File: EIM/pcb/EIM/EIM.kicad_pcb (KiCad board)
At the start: 2 copper layers, 170.6 x 136.2 mm, 249 parts, among them IC1 TLIN1027DRQ1, IC10 ILD213T, IC2 SN65HVD1780QDRQ1, IC3 ILD213T, IC4 ILD213T, IC5 ILD213T, IC6 ILD213T, IC7 ILD213T, IC8 ILD213T, IC9 ILD213T, J1 MX34028NF2, J2 36783-1201, J3 34830-0801, J4 34830-2001, J5 DEBUG1, J6 DEBUG2, J7 FTSH-107-01-F-DV-K, J8 SWD, K1 G8N-1L-AS_DC12, Q1 BSS138, Q2 BSS138, Q3 BSS138, Q4 BSS138, Q5 BSS138, Q6 BSS138, Q7 BSS138, SW1 BOOT, SW2 RESET, U1 STM32F429ZITx, U10 BTS6142D, U11 BTS6142D, U12 BTS6142D, U2 AP63200WU, U3 AP63203WU, U4 SN65HVD233, U5 SN65HVD233, U6 BTS6142D, U7 BTS6142D, U8 BTS6142D, U9 BTS6142D, X1 ASE-8.000MHz, X2 ECS-327-32.768kHz

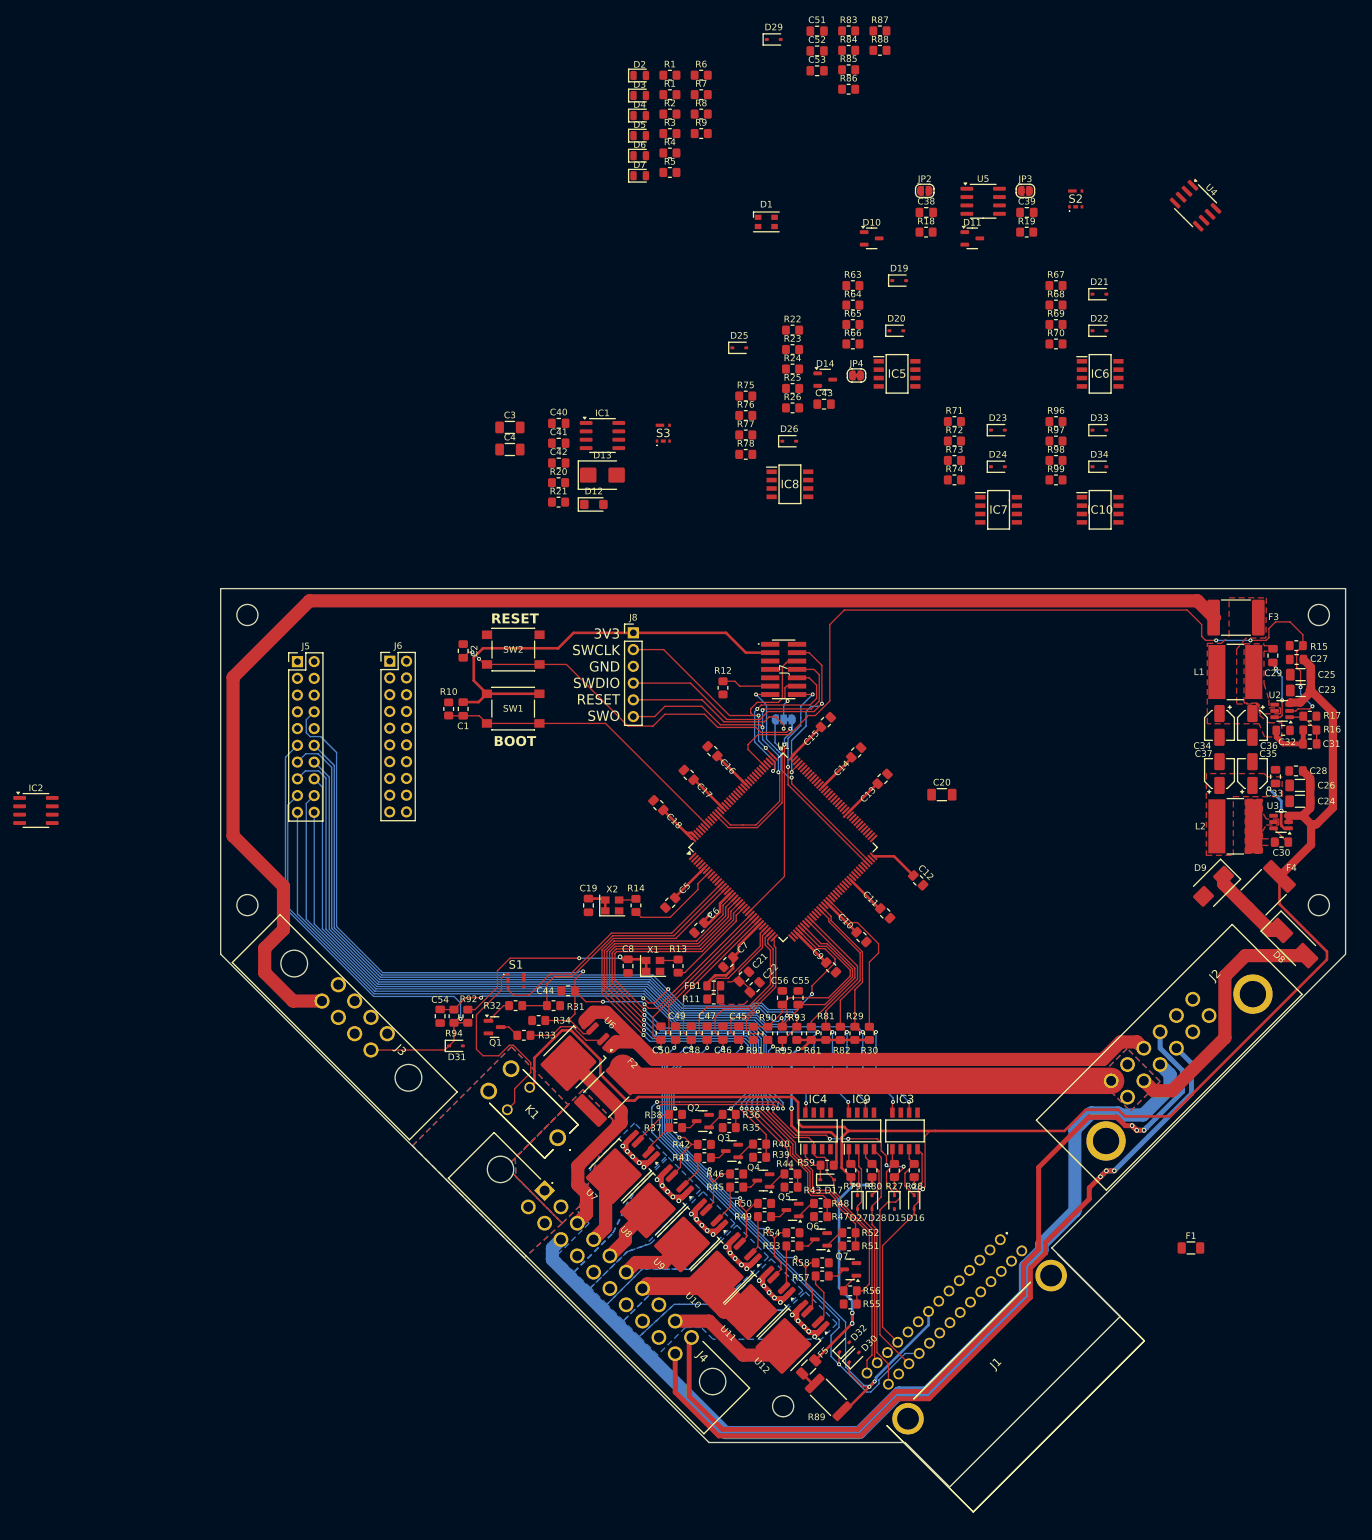
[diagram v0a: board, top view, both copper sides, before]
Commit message: All components placed and pins assigned.
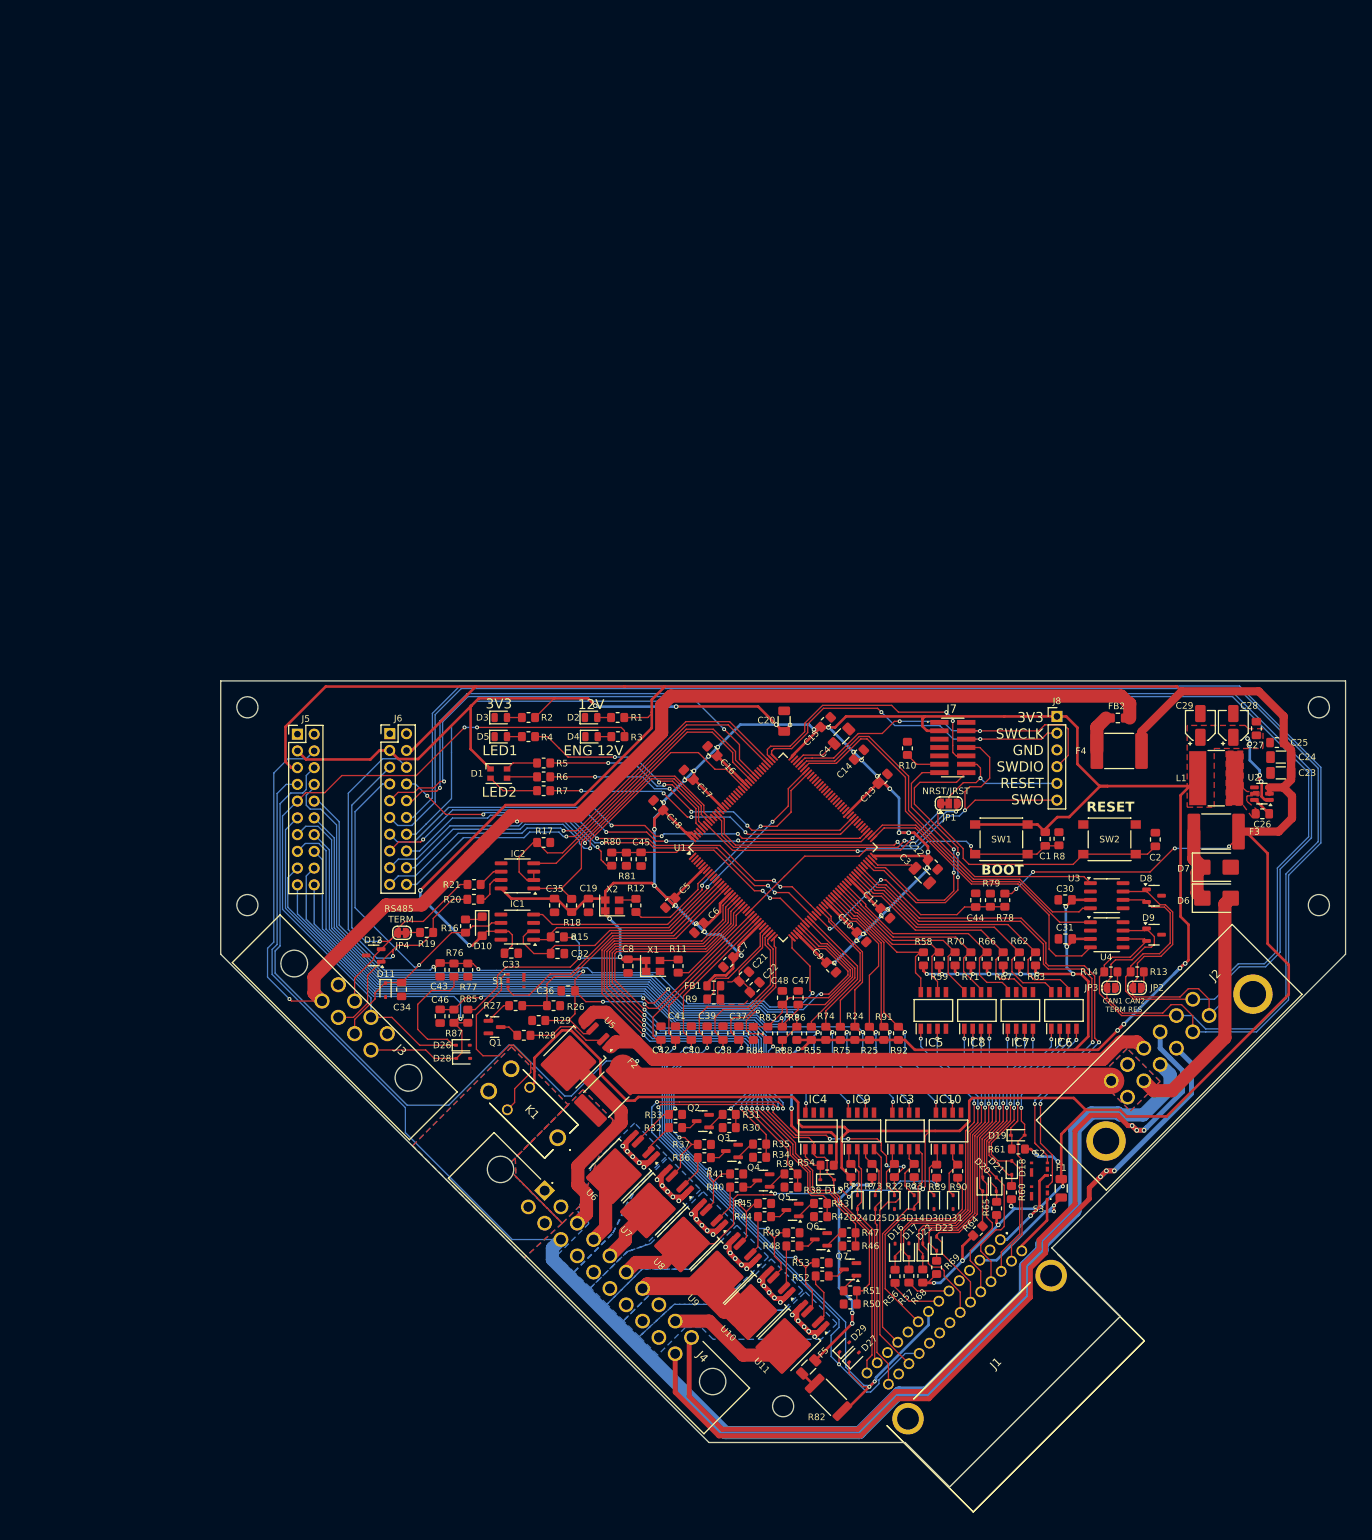
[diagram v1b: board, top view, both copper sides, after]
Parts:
- removed the C23 at (191.8, 66.2)
- removed the C25 at (191.8, 63.8)
- removed the C27 at (191.2, 61.5)
- removed the C29 at (187.6, 60.9)
- removed the C31 at (193.2, 74.3)
- removed the C32 at (189.2, 72.2)
- removed the C34 at (179.5, 71.5)
- removed the C36 at (184.5, 71.5)
- removed C53: 100n, Capacitor_SMD:C_0805_2012Metric_Pad1.18x1.45mm_HandSolder
- removed the D13 at (85.9, 33.5)
- removed the D3 at (91.6, -24.0)
- removed the D5 at (91.6, -17.9)
- removed the F3 at (182.0, 55.1)
- removed the L1 at (181.9, 63.4)
- removed the R1 at (96.2, -27.1)
- removed the R15 at (191.2, 59.4)
- removed the R16 at (193.2, 72.2)
- removed the R17 at (193.2, 70.1)
- removed the R2 at (96.2, -21.2)
- removed the R4 at (96.2, -15.3)
- removed the R87 at (128.0, -33.8)
- removed the R88 at (128.0, -30.9)
- removed the U2 at (189.0, 69.3)
- added C45: 100n, Capacitor_SMD:C_0805_2012Metric_Pad1.18x1.45mm_HandSolder, F.Cu at (91.8, 91.8)
- added D11: SD15-01FTG, Diode_SMD:D_SOD-323, F.Cu at (53.0, 111.7)
- added F4: 2920L260/33DR, Fuse:Fuse_2920_7451Metric, F.Cu at (164.3, 75.4)
- added FB2: 220ohm / 10MHZ, Inductor_SMD:L_0805_2012Metric_Pad1.15x1.40mm_HandSolder, F.Cu at (164.1, 70.4)
- added R80: 3k6, 0.5%, Resistor_SMD:R_0805_2012Metric_Pad1.20x1.40mm_HandSolder, F.Cu at (87.3, 91.8)
- added R81: 1k, 0.5%, Resistor_SMD:R_0805_2012Metric_Pad1.20x1.40mm_HandSolder, F.Cu at (89.5, 91.8)
- D6: renamed from D8; footprint Diode_SMD:D_SMB_Handsoldering -> Diode_SMD:D_SMB
- IC2: value SN65HVD1780QDRQ1 -> ISL3172EIBZ
- JP1: moved to F.Cu
- moved D26 159.7 mm to (64.8, 120.0)
- moved R76 154.5 mm to (63.4, 108.6), turned to 90 degrees
- moved C43 153.4 mm to (61.3, 108.6), turned to -90 degrees
- moved R77 151.0 mm to (65.5, 108.6), turned to -90 degrees
- moved R56 150.4 mm to (130.3, 155.1), turned to 90 degrees
- moved R57 147.5 mm to (132.4, 155.0), turned to 90 degrees
- moved S2 147.3 mm to (152.2, 138.8), turned to 90 degrees
- moved D16 147.1 mm to (130.3, 151.2), turned to 90 degrees
- moved D22 139.7 mm to (134.5, 151.1), turned to 90 degrees
- moved D17 139.5 mm to (132.4, 151.1), turned to 90 degrees
- moved R60 137.7 mm to (147.9, 142.3), turned to 90 degrees
- moved R68 136.1 mm to (134.5, 155.0), turned to 90 degrees
- moved D18 133.2 mm to (148.0, 138.6), turned to 90 degrees
- moved R69 132.4 mm to (136.6, 153.7), turned to 90 degrees
- moved C44 131.0 mm to (142.5, 98.0), turned to 90 degrees
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- renumbered C24 to C23, C26 to C24, C28 to C25, C30 to C26, C33 to C27, C35 to C28, C37 to C29, C38 to C30, C39 to C31, C40 to C32, C41 to C33, C42 to C34, C43 to C35, C44 to C36, C45 to C37, C46 to C38, C47 to C39, C48 to C40, C49 to C41, C50 to C42, C51 to C43, C52 to C44, C54 to C46, C55 to C47, C56 to C48, D12 to D10, D14 to D12, D15 to D13, D16 to D14, D17 to D15, D19 to D16, D20 to D17, D21 to D18, D22 to D19, D23 to D20, D24 to D21, D25 to D22, D26 to D23, D27 to D24, D28 to D25, D29 to D26, D30 to D27, D31 to D28, D32 to D29, D4 to D3, D33 to D30, D34 to D31, D6 to D4, D7 to D5, D9 to D7, D10 to D8, D11 to D9, F4 to F3, L2 to L1, R12 to R10, R13 to R11, R14 to R12, R18 to R13, R19 to R14, R20 to R15, R21 to R16, R22 to R17, R23 to R18, R24 to R19, R3 to R2, R25 to R20, R26 to R21, R27 to R22, R28 to R23, R29 to R24, R30 to R25, R31 to R26, R32 to R27, R33 to R28, R34 to R29, R5 to R3, R35 to R30, R36 to R31, R37 to R32, R38 to R33, R39 to R34, R40 to R35, R41 to R36, R42 to R37, R43 to R38, R44 to R39, R6 to R4, R45 to R40, R46 to R41, R47 to R42, R48 to R43, R49 to R44, R50 to R45, R51 to R46, R52 to R47, R53 to R48, R54 to R49, R7 to R5, R55 to R50, R56 to R51, R57 to R52, R58 to R53, R59 to R54, R61 to R55, R63 to R56, R64 to R57, R65 to R58, R66 to R59, R8 to R6, R67 to R60, R68 to R61, R69 to R62, R70 to R63, R71 to R64, R72 to R65, R73 to R66, R74 to R67, R75 to R68, R76 to R69, R9 to R7, R77 to R70, R78 to R71, R79 to R72, R80 to R73, R81 to R74, R82 to R75, R83 to R76, R84 to R77, R85 to R78, R86 to R79, R10 to R8, R89 to R82, R90 to R83, R91 to R84, R92 to R85, R93 to R86, R94 to R87, R95 to R88, R96 to R89, R11 to R9, R97 to R90, R98 to R91, R99 to R92, U11 to U10, U12 to U11, U3 to U2, U4 to U3, U5 to U4, U6 to U5, U7 to U6, U8 to U7, U9 to U8, U10 to U9
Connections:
- D18 pad 2: /1ST -> /2ND
- D19 pad 2: /2ND -> /1ST
- D20 pad 2: /3RD -> /4TH
- D21 pad 2: /4TH -> /3RD
- D22 pad 2: /5TH -> /6TH
- D23 pad 2: /6TH -> /5TH
- IC5 pad 6: /TURN_L_MCU -> /TURN_R_MCU
- IC5 pad 8: /TURN_R_MCU -> /TURN_L_MCU
- IC6 pad 2: /1ST -> /2ND
- IC6 pad 4: /2ND -> /1ST
- IC6 pad 6: /2ND_MCU -> /1ST_MCU
- IC6 pad 8: /1ST_MCU -> /2ND_MCU
- IC7 pad 2: /3RD -> /4TH
- IC7 pad 4: /4TH -> /3RD
- IC7 pad 6: /4TH_MCU -> /3RD_MCU
- IC7 pad 8: /3RD_MCU -> /4TH_MCU
- IC8 pad 2: /5TH -> /6TH
- IC8 pad 4: /6TH -> /5TH
- IC8 pad 6: /6TH_MCU -> /5TH_MCU
- IC8 pad 8: /5TH_MCU -> /6TH_MCU
- J2 pad 11: /CAN1_H -> /CAN2_H
- J2 pad 12: /CAN2_H -> /CAN1_H
- J2 pad 5: /CAN1_L -> /CAN2_L
- J2 pad 6: /CAN2_L -> /CAN1_L
- J3 pad 5: /SERVO_8V -> /SERVO_12V
- J5 pad 4: +8V -> /SERVO_12V
- R5 pad 2: /LED_B -> /LED2_B
- R56 pad 1: /TURN_R -> /TURN_L
- R57 pad 1: /TURN_L -> /TURN_R
- R58 pad 1: /TURN_R_MCU -> /TURN_L_MCU
- R59 pad 1: /TURN_L_MCU -> /TURN_R_MCU
- R6 pad 2: /LED_G -> /LED2_G
- R62 pad 1: /1ST_MCU -> /2ND_MCU
- R63 pad 1: /2ND_MCU -> /1ST_MCU
- R66 pad 1: /3RD_MCU -> /4TH_MCU
- R67 pad 1: /4TH_MCU -> /3RD_MCU
- R7 pad 2: /LED_R -> /LED2_R
- R70 pad 1: /5TH_MCU -> /6TH_MCU
- R71 pad 1: /6TH_MCU -> /5TH_MCU
- U1 pad 100: /KLINE_EN -> unconnected-(U1-PA8-Pad100)
- U1 pad 113: /8V_EN -> unconnected-(U1-PC12-Pad113)
- U1 pad 12: unconnected-(U1-PF2-Pad12) -> /KLINE_EN
- U1 pad 139: unconnected-(U1-PB8-Pad139) -> /LED1
- U1 pad 140: unconnected-(U1-PB9-Pad140) -> /LED2_B
- U1 pad 43: /8V_ADC -> /SERVO_12V_ADC
- U1 pad 54: unconnected-(U1-PF14-Pad54) -> /LOWBEAM_MCU
- U1 pad 55: unconnected-(U1-PF15-Pad55) -> /HIGHBEAM_MCU
- U1 pad 56: unconnected-(U1-PG0-Pad56) -> /TURN_L_MCU
- U1 pad 57: unconnected-(U1-PG1-Pad57) -> /TURN_R_MCU
- U1 pad 58: unconnected-(U1-PE7-Pad58) -> /6TH_MCU
- U1 pad 59: unconnected-(U1-PE8-Pad59) -> /5TH_MCU
- U1 pad 60: unconnected-(U1-PE9-Pad60) -> /4TH_MCU
- U1 pad 63: unconnected-(U1-PE10-Pad63) -> /3RD_MCU
- U1 pad 64: unconnected-(U1-PE11-Pad64) -> /2ND_MCU
- U1 pad 65: unconnected-(U1-PE12-Pad65) -> /1ST_MCU
- U1 pad 66: unconnected-(U1-PE13-Pad66) -> /HL_RLY_EN
- U1 pad 67: unconnected-(U1-PE14-Pad67) -> /LAP_RLY_EN
- U1 pad 81: unconnected-(U1-PD12-Pad81) -> /LED2_R
- U1 pad 82: unconnected-(U1-PD13-Pad82) -> /LED2_G
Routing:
- net +3V3: track 243.3 -> 711.1 mm, vias 7 -> 55
- net +12V: track 278.3 -> 625.9 mm, vias 6 -> 19
- net /CAN2_H: track 0.00 -> 250.9 mm
- net /CAN2_L: track 0.00 -> 248.8 mm
- net /CAN1_H: track 0.00 -> 241.9 mm, vias 0 -> 1
- net /CAN1_L: track 0.00 -> 236.9 mm, vias 0 -> 1
- net /SERVO_12V: track 0.00 -> 220.3 mm, vias 0 -> 3
- net /SERVO_8V: track 214.4 -> 0.00 mm
- net /ENG_12V_ON_SENSE: track 0.00 -> 128.0 mm, vias 0 -> 2
- net /8V_EN: track 125.6 -> 0.00 mm, vias 4 -> 0
- net /ENG_12V_ADC: track 0.00 -> 109.8 mm, vias 0 -> 3
- net /KEYSWITCH_FEED: track 75.0 -> 184.7 mm, vias 0 -> 1
- net /ENG_ON_RLY_RTN: track 144.4 -> 238.5 mm
- net /LAP_RLY_EN: track 0.00 -> 80.9 mm, vias 0 -> 2
- net /SPI2_MISO: track 0.00 -> 77.8 mm, vias 0 -> 4
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- removed copper zone on F.Cu, net +8V
- removed copper zone on F.Cu, net /Power Supply/8V_BUCK_OUT
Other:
- board size 170.6 x 136.2 mm -> 170.6 x 122.2 mm
- board text added: "12V"
- board text added: "3V3"
- board text added: "CAN1 CAN2 TERM RES"
- board text added: "ENG 12V"
- board text added: "LED1"
- board text added: "LED2"
- board text added: "RS485 TERM"

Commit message: EIM board complete - awaiting DR
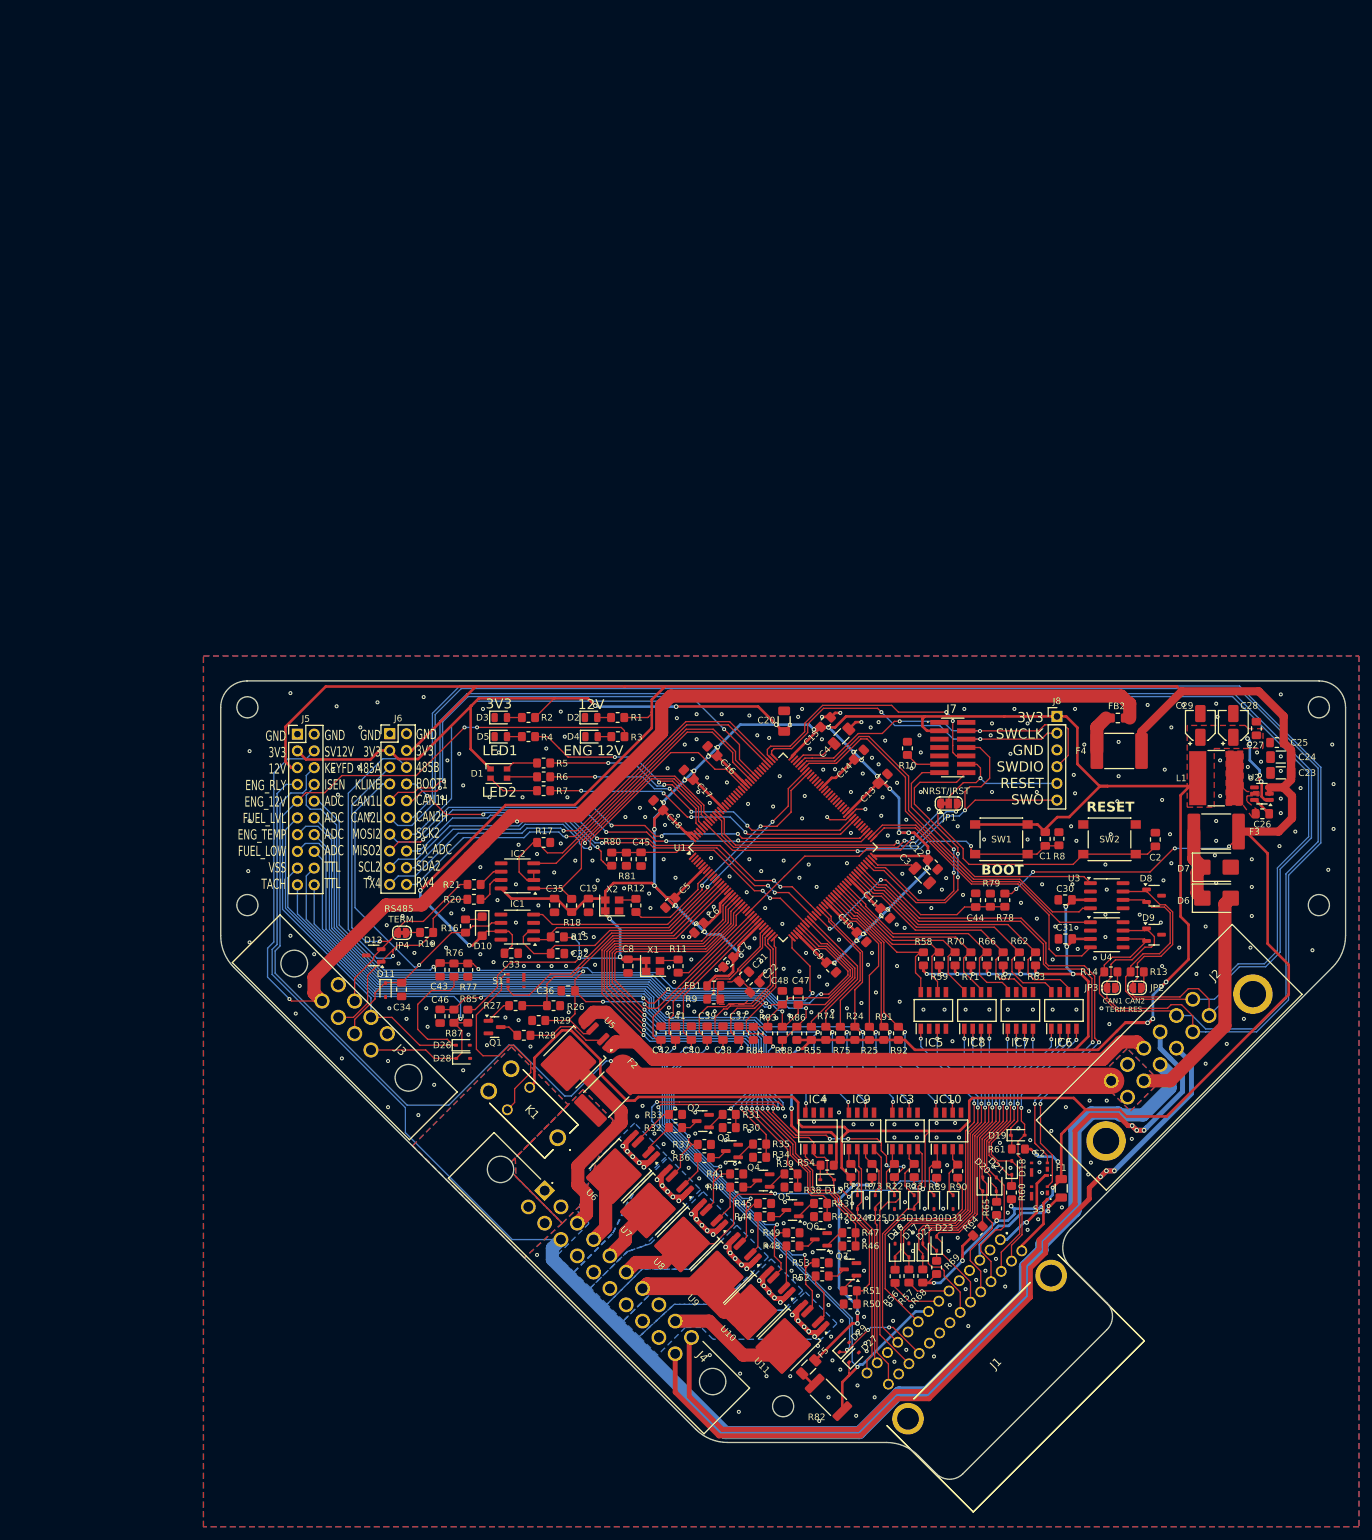
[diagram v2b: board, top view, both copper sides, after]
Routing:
- net GND: track 0.00 -> 17.4 mm, vias 0 -> 407
- net +3V3: track 711.1 -> 721.5 mm
- net /FUEL_LOW: track 209.7 -> 204.5 mm, vias 6 -> 5
- net /KEYSWITCH_FEED: track 184.7 -> 180.3 mm
- net /FUEL_LOW_ADC: track 121.0 -> 116.8 mm
- net /TEMP: track 204.0 -> 201.2 mm, vias 5 -> 7
- net /KEYSWITCH_RTN: track 37.8 -> 35.5 mm
- net /FUEL_LVL_ADC: track 150.9 -> 149.7 mm
- net /ENG_12V_ADC: track 109.8 -> 108.7 mm
- net /HIGHBEAM_I_SEN: track 61.4 -> 62.5 mm
- net /TACH_MCU: track 132.7 -> 133.7 mm
- net /SP_SIG: track 147.0 -> 148.0 mm
- net +12V: track 625.9 -> 626.9 mm
- net /VSS_MCU: track 129.3 -> 130.3 mm
- net /TA_SIG: track 154.5 -> 155.5 mm
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- added copper zone on B.Cu, net GND
- added copper zone on F.Cu, net GND
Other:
- board size 170.6 x 122.2 mm -> 170.6 x 121.1 mm
- board text added: "GND 3V3 12V ENG_RLY ENG_12V FUEL_LVL ENG_TEMP FUEL_LOW VSS TACH"
- board text added: "GND 3V3 485A KLINE CAN1L CAN2L MOSI2 MISO2 SCL2 TX4"
- board text added: "GND 3V3 485B BOOT1 CAN1H CAN2H SCK2 EX_ADC SDA2 RX4"
- board text added: "GND SV12V KEYFD ISEN ADC ADC ADC ADC TTL TTL"

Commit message: Updated small things to make DRC pass without errors or warnings
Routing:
- net /FUEL_LOW: track 204.5 -> 210.9 mm, vias 5 -> 6
- net GND: track 17.4 -> 20.0 mm, vias 407 -> 412
- net /TEMP: track 201.2 -> 202.6 mm
- net /SP_SIG: track 148.0 -> 149.3 mm
- net /OIL: track 37.3 -> 38.2 mm
- net /FAULT_IND: track 34.1 -> 35.1 mm
- net /LAP_RLY_EN: track 80.9 -> 81.7 mm
- net +3V3: track 721.5 -> 722.3 mm
- net /TA_SIG: track 155.5 -> 154.7 mm
- net +12V: track 626.9 -> 627.7 mm
- net /CAN1_RX: track 59.4 -> 60.0 mm
- net /CAN1_TX: track 58.0 -> 58.5 mm
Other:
- outline, holes or cut-outs redrawn
- board text added: "BLUE CAR EIM rev 1 1/14/24"

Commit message: Board data as ordered on 1-15-25
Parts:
- R10: value 100R -> 120R
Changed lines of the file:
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@@
 			)
 		)
-		(property "Value" "100R"
+		(property "Value" "120R"
 			(at 0 1.65 90)
 			(layer "F.Fab")
